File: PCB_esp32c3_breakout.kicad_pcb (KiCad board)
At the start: 2 copper layers, 19.6 x 44.5 mm, 4 parts, among them J1 Conn_01x09_Pin, J2 Conn_01x09_Pin, U1 ESP32-C3-WROOM-02

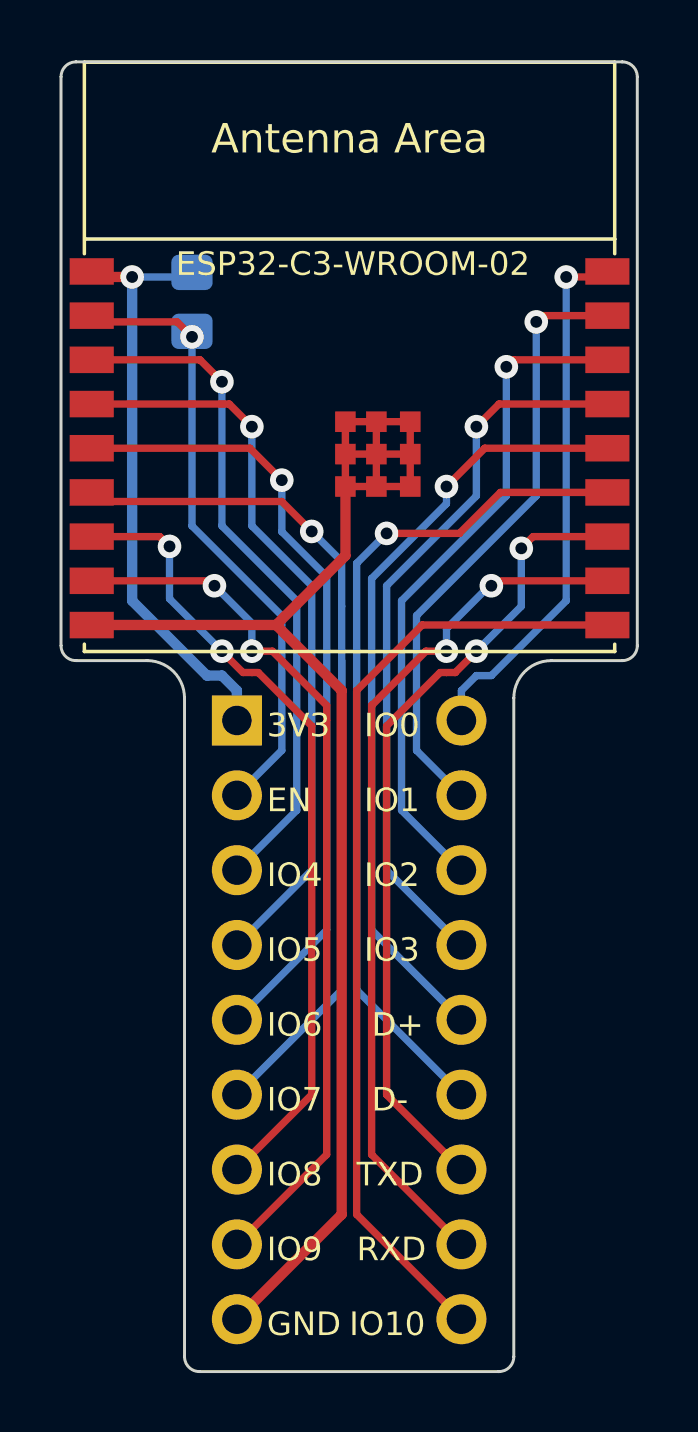
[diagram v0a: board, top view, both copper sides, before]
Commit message: Adjust board size
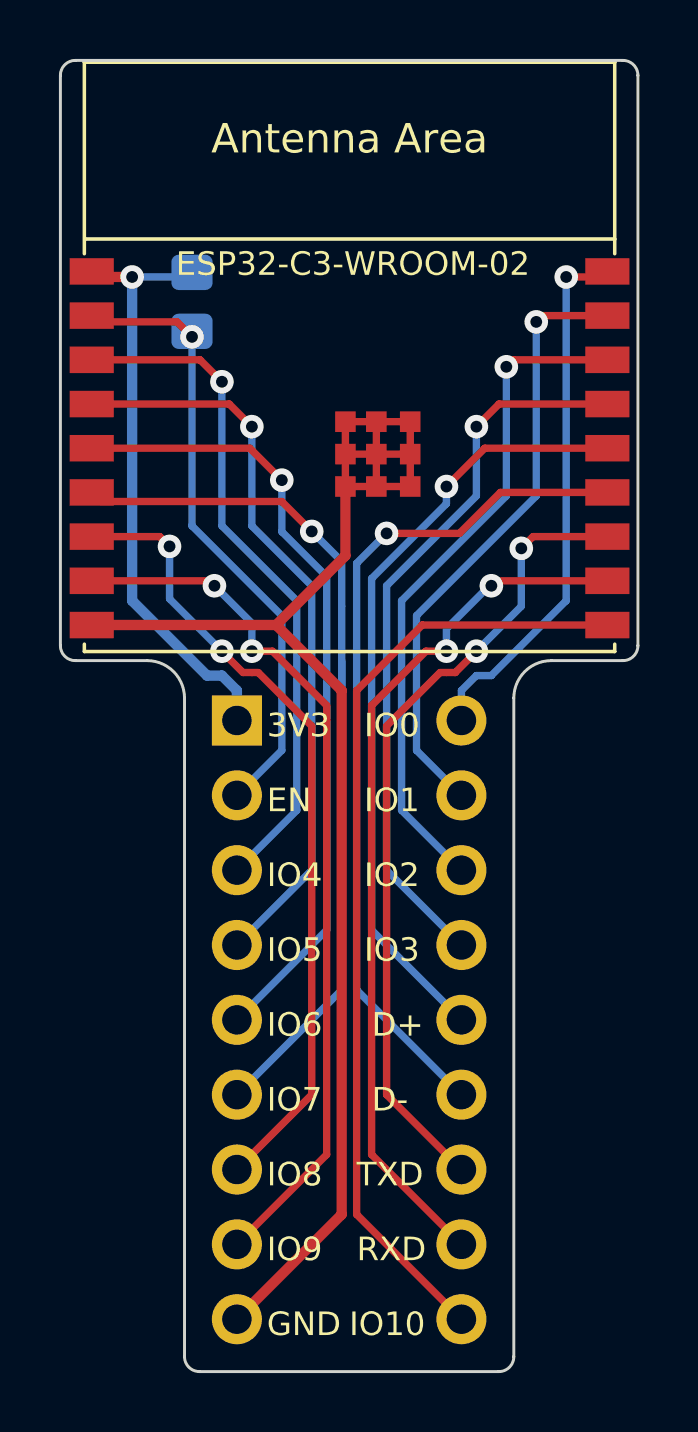
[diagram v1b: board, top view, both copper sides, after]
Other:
- outline, holes or cut-outs redrawn
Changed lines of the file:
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@@
     )
   )
-  (gr_arc (start 79.629 58.42) (mid 79.48021 58.77921) (end 79.121 58.928)
+  (gr_arc (start 79.65 58.42) (mid 79.501211 58.779211) (end 79.142 58.928)
     (stroke (width 0.1) (type default)) (layer "Edge.Cuts"))
   (gr_line (start 64.77 83.058) (end 74.93 83.058)
     (stroke (width 0.1) (type default)) (layer "Edge.Cuts"))
-  (gr_line (start 76.708 58.928) (end 79.121 58.928)
+  (gr_line (start 76.708 58.928) (end 79.142 58.928)
     (stroke (width 0.1) (type default)) (layer "Edge.Cuts"))
   (gr_arc (start 64.77 83.058) (mid 64.41079 82.90921) (end 64.262 82.55)
     (stroke (width 0.1) (type default)) (layer "Edge.Cuts"))
-  (gr_arc (start 60.579 58.928) (mid 60.21979 58.77921) (end 60.071 58.42)
+  (gr_arc (start 60.558 58.928) (mid 60.198789 58.779211) (end 60.05 58.42)
     (stroke (width 0.1) (type default)) (layer "Edge.Cuts"))
-  (gr_line (start 79.629 58.42) (end 79.629 39.116)
+  (gr_line (start 79.65 58.42) (end 79.65 39.066)
     (stroke (width 0.1) (type default)) (layer "Edge.Cuts"))
   (gr_arc (start 75.438 82.55) (mid 75.28921 82.90921) (end 74.93 83.058)
     (stroke (width 0.1) (type default)) (layer "Edge.Cuts"))
-  (gr_line (start 60.579 58.928) (end 62.992 58.928)
+  (gr_line (start 60.558 58.928) (end 62.992 58.928)
     (stroke (width 0.1) (type default)) (layer "Edge.Cuts"))
   (gr_line (start 64.262 60.198) (end 64.262 82.55)
     (stroke (width 0.1) (type default)) (layer "Edge.Cuts"))
-  (gr_line (start 79.121 38.608) (end 60.579 38.608)
+  (gr_line (start 79.142 38.558) (end 60.558 38.558)
     (stroke (width 0.1) (type default)) (layer "Edge.Cuts"))
-  (gr_line (start 60.071 39.116) (end 60.071 58.42)
+  (gr_line (start 60.05 39.066) (end 60.05 58.42)
     (stroke (width 0.1) (type default)) (layer "Edge.Cuts"))
-  (gr_arc (start 60.071 39.116) (mid 60.21979 38.75679) (end 60.579 38.608)
+  (gr_arc (start 60.05 39.066) (mid 60.198789 38.706789) (end 60.558 38.558)
     (stroke (width 0.1) (type default)) (layer "Edge.Cuts"))
   (gr_arc (start 75.438 60.198) (mid 75.809974 59.299974) (end 76.708 58.928)
@@
   (gr_line (start 75.438 82.55) (end 75.438 60.198)
     (stroke (width 0.1) (type default)) (layer "Edge.Cuts"))
-  (gr_arc (start 79.121 38.608) (mid 79.48021 38.75679) (end 79.629 39.116)
+  (gr_arc (start 79.142 38.558) (mid 79.501211 38.706789) (end 79.65 39.066)
     (stroke (width 0.1) (type default)) (layer "Edge.Cuts"))
   (gr_arc (start 62.992 58.928) (mid 63.890026 59.299974) (end 64.262 60.198)
@@
   )
   (dimension (type aligned) (layer "Dwgs.User")
-    (pts (xy 60.071 39.116) (xy 79.629 39.116))
-    (height -2.413)
-    (gr_text "19.5580 mm" (at 69.85 35.553) (layer "Dwgs.User")
+    (pts (xy 60.05 39.054) (xy 79.65 39.054))
+    (height -2.478)
+    (gr_text "19.6000 mm" (at 69.85 35.426) (layer "Dwgs.User")
       (effects (font (size 1 1) (thickness 0.15)))
     )
@@
   )
   (dimension (type aligned) (layer "Dwgs.User")
-    (pts (xy 69.863 38.62) (xy 69.85 83.058))
-    (height 11.728022)
-    (gr_text "44.4380 mm" (at 56.978479 60.835233 89.98323855) (layer "Dwgs.User")
+    (pts (xy 69.85 83.058) (xy 69.85 38.558))
+    (height -11.938)
+    (gr_text "44.5000 mm" (at 56.762 60.808 90) (layer "Dwgs.User")
       (effects (font (size 1 1) (thickness 0.15)))
     )

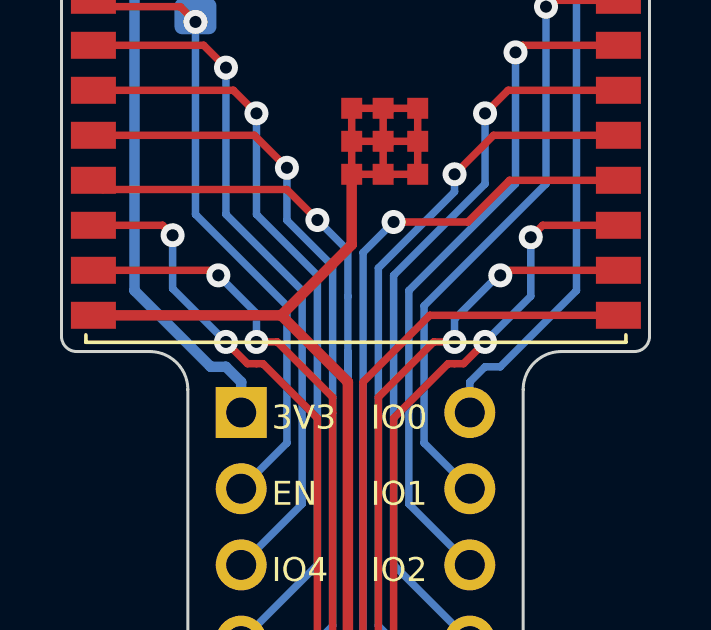
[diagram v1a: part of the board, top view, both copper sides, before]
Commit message: Change JLCJLCJLCJLC to WayWayWay
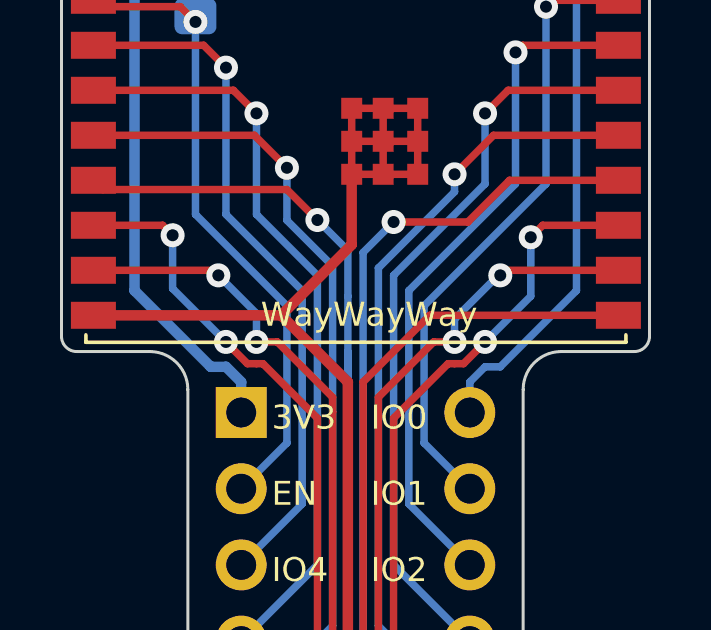
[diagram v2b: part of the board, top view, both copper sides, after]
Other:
- board text added: "WayWayWay"
- board text removed: "JLCJLCJLCJLC"
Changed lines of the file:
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@@
     (effects (font (size 0.8 0.8) (thickness 0.13)) (justify bottom mirror))
-  )
-  (gr_text "JLCJLCJLCJLC" (at 73.914 58.166) (layer "B.SilkS")
-    (effects (font (size 0.8 0.8) (thickness 0.15)) (justify left bottom mirror))
   )
   (gr_text "D+" (at 70.612 71.755) (layer "F.SilkS")
@@
     (effects (font (size 0.8 0.8) (thickness 0.13)) (justify left bottom))
   )
+  (gr_text "WayWayWay" (at 73.914 58.166) (layer "F.SilkS")
+    (effects (font (size 0.8 0.8) (thickness 0.15)) (justify right bottom))
+  )
   (gr_text "EN" (at 67.056 64.135) (layer "F.SilkS")
